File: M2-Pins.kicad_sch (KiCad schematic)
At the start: 5 parts, among them J3 M.2-M+B-Pins

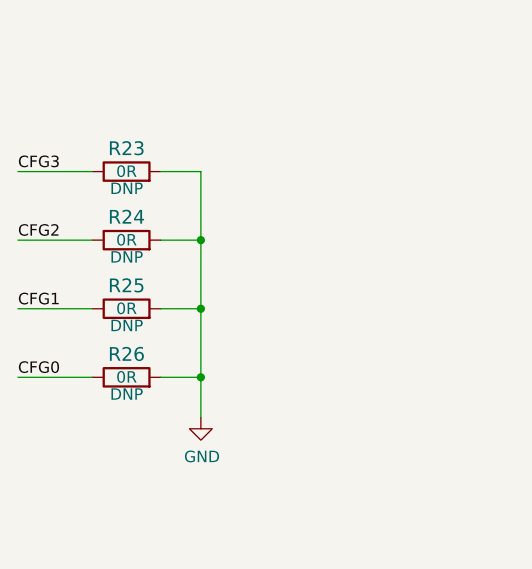
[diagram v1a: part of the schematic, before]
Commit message: [#102286] Fix legacy DNP
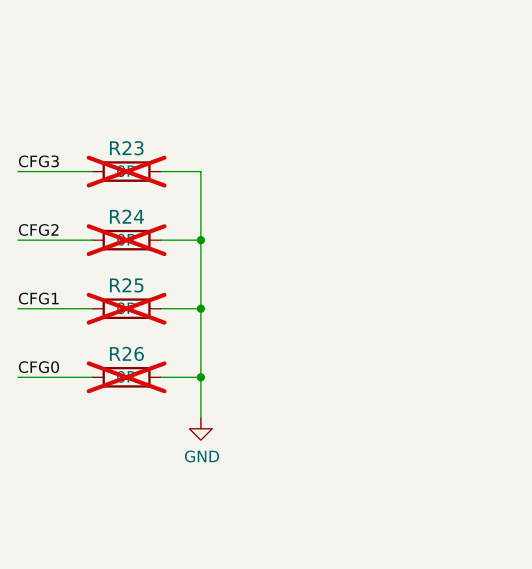
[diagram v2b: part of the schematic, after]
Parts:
- R23, R24, R25, R26: DNP DNP -> (none); now not fitted
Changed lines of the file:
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@@
 		(on_board yes)
 		(in_pos_files yes)
-		(dnp no)
+		(dnp yes)
 		(property "Reference" "R23"
 			(at 130.175 83.185 0)
@@
 		(property "Val" "0R"
 			(at 130.175 85.725 0)
-			(show_name no)
-			(do_not_autoplace no)
-			(effects
-				(font
-					(size 1.27 1.27)
-				)
-			)
-		)
-		(property "DNP" "DNP"
-			(at 130.175 87.63 0)
 			(show_name no)
 			(do_not_autoplace no)
@@
 		(on_board yes)
 		(in_pos_files yes)
-		(dnp no)
+		(dnp yes)
 		(property "Reference" "R24"
 			(at 130.175 90.805 0)
@@
 		(property "Val" "0R"
 			(at 130.175 93.345 0)
-			(show_name no)
-			(do_not_autoplace no)
-			(effects
-				(font
-					(size 1.27 1.27)
-				)
-			)
-		)
-		(property "DNP" "DNP"
-			(at 130.175 95.25 0)
 			(show_name no)
 			(do_not_autoplace no)
@@
 		(on_board yes)
 		(in_pos_files yes)
-		(dnp no)
+		(dnp yes)
 		(property "Reference" "R25"
 			(at 130.175 98.425 0)
@@
 		(property "Val" "0R"
 			(at 130.175 100.965 0)
-			(show_name no)
-			(do_not_autoplace no)
-			(effects
-				(font
-					(size 1.27 1.27)
-				)
-			)
-		)
-		(property "DNP" "DNP"
-			(at 130.175 102.87 0)
 			(show_name no)
 			(do_not_autoplace no)
@@
 		(on_board yes)
 		(in_pos_files yes)
-		(dnp no)
+		(dnp yes)
 		(property "Reference" "R26"
 			(at 130.175 106.045 0)
@@
 			(show_name no)
 			(do_not_autoplace no)
-			(effects
-				(font
-					(size 1.27 1.27)
-				)
-			)
-		)
-		(property "DNP" "DNP"
-			(at 130.175 110.49 0)
-			(show_name no)
-			(do_not_autoplace no)

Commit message: [#102286] Set exclude from BOM & pnp for J3
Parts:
- J3: now left out of the parts list
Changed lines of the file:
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@@
 		)
 		(property "Intersheetrefs" "${INTERSHEET_REFS}"
-			(at 0 0 0)
-			(hide yes)
-			(show_name no)
-			(do_not_autoplace no)
-			(effects
-				(font
-					(size 1.27 1.27)
-				)
+			(at 165.7929 142.24 0)
+			(hide yes)
+			(show_name no)
+			(do_not_autoplace no)
+			(effects
+				(font
+					(size 1.27 1.27)
+				)
+				(justify right)
 			)
 		)
@@
 		)
 		(property "Intersheetrefs" "${INTERSHEET_REFS}"
-			(at 0 0 0)
-			(hide yes)
-			(show_name no)
-			(do_not_autoplace no)
-			(effects
-				(font
-					(size 1.27 1.27)
-				)
+			(at 165.3393 157.48 0)
+			(hide yes)
+			(show_name no)
+			(do_not_autoplace no)
+			(effects
+				(font
+					(size 1.27 1.27)
+				)
+				(justify right)
 			)
 		)
@@
 		)
 		(property "Intersheetrefs" "${INTERSHEET_REFS}"
-			(at 0 0 0)
-			(hide yes)
-			(show_name no)
-			(do_not_autoplace no)
-			(effects
-				(font
-					(size 1.27 1.27)
-				)
+			(at 284.0895 153.67 0)
+			(hide yes)
+			(show_name no)
+			(do_not_autoplace no)
+			(effects
+				(font
+					(size 1.27 1.27)
+				)
+				(justify left)
 			)
 		)
@@
 		)
 		(property "Intersheetrefs" "${INTERSHEET_REFS}"
-			(at 0 0 0)
-			(hide yes)
-			(show_name no)
-			(do_not_autoplace no)
-			(effects
-				(font
-					(size 1.27 1.27)
-				)
+			(at 275.139 156.21 0)
+			(hide yes)
+			(show_name no)
+			(do_not_autoplace no)
+			(effects
+				(font
+					(size 1.27 1.27)
+				)
+				(justify left)
 			)
 		)
@@
 		)
 		(property "Intersheetrefs" "${INTERSHEET_REFS}"
-			(at 0 0 0)
-			(hide yes)
-			(show_name no)
-			(do_not_autoplace no)
-			(effects
-				(font
-					(size 1.27 1.27)
-				)
+			(at 273.6271 151.13 0)
+			(hide yes)
+			(show_name no)
+			(do_not_autoplace no)
+			(effects
+				(font
+					(size 1.27 1.27)
+				)
+				(justify left)
 			)
 		)
@@
 		)
 		(property "Intersheetrefs" "${INTERSHEET_REFS}"
-			(at 0 0 0)
-			(hide yes)
-			(show_name no)
-			(do_not_autoplace no)
-			(effects
-				(font
-					(size 1.27 1.27)
-				)
+			(at 261.7436 90.17 0)
+			(hide yes)
+			(show_name no)
+			(do_not_autoplace no)
+			(effects
+				(font
+					(size 1.27 1.27)
+				)
+				(justify left)
 			)
 		)
@@
 		)
 		(property "Intersheetrefs" "${INTERSHEET_REFS}"
-			(at 0 0 0)
-			(hide yes)
-			(show_name no)
-			(do_not_autoplace no)
-			(effects
-				(font
-					(size 1.27 1.27)
-				)
+			(at 165.2788 154.94 0)
+			(hide yes)
+			(show_name no)
+			(do_not_autoplace no)
+			(effects
+				(font
+					(size 1.27 1.27)
+				)
+				(justify right)
 			)
 		)
@@
 		)
 		(property "Intersheetrefs" "${INTERSHEET_REFS}"
-			(at 0 0 0)
-			(hide yes)
-			(show_name no)
-			(do_not_autoplace no)
-			(effects
-				(font
-					(size 1.27 1.27)
-				)
+			(at 165.7324 139.7 0)
+			(hide yes)
+			(show_name no)
+			(do_not_autoplace no)
+			(effects
+				(font
+					(size 1.27 1.27)
+				)
+				(justify right)
 			)
 		)
@@
 		)
 		(property "Intersheetrefs" "${INTERSHEET_REFS}"
-			(at 0 0 0)
-			(hide yes)
-			(show_name no)
-			(do_not_autoplace no)
-			(effects
-				(font
-					(size 1.27 1.27)
-				)
+			(at 166.0348 147.32 0)
+			(hide yes)
+			(show_name no)
+			(do_not_autoplace no)
+			(effects
+				(font
+					(size 1.27 1.27)
+				)
+				(justify right)
 			)
 		)
@@
 		)
 		(property "Intersheetrefs" "${INTERSHEET_REFS}"
-			(at 0 0 0)
-			(hide yes)
-			(show_name no)
-			(do_not_autoplace no)
-			(effects
-				(font
-					(size 1.27 1.27)
-				)
+			(at 166.0953 149.86 0)
+			(hide yes)
+			(show_name no)
+			(do_not_autoplace no)
+			(effects
+				(font
+					(size 1.27 1.27)
+				)
+				(justify right)
 			)
 		)
@@
 		)
 		(property "Intersheetrefs" "${INTERSHEET_REFS}"
-			(at 0 0 0)
-			(hide yes)
-			(show_name no)
-			(do_not_autoplace no)
-			(effects
-				(font
-					(size 1.27 1.27)
-				)
+			(at 257.9336 181.61 0)
+			(hide yes)
+			(show_name no)
+			(do_not_autoplace no)
+			(effects
+				(font
+					(size 1.27 1.27)
+				)
+				(justify left)
 			)
 		)
@@
 		(body_style 1)
 		(exclude_from_sim no)
-		(in_bom yes)
+		(in_bom no)
 		(on_board yes)
-		(in_pos_files yes)
+		(in_pos_files no)
 		(dnp no)
 		(property "Reference" "J3"
